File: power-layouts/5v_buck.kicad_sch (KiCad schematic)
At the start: 24 parts, among them U801 MIC28517T-E/PHA

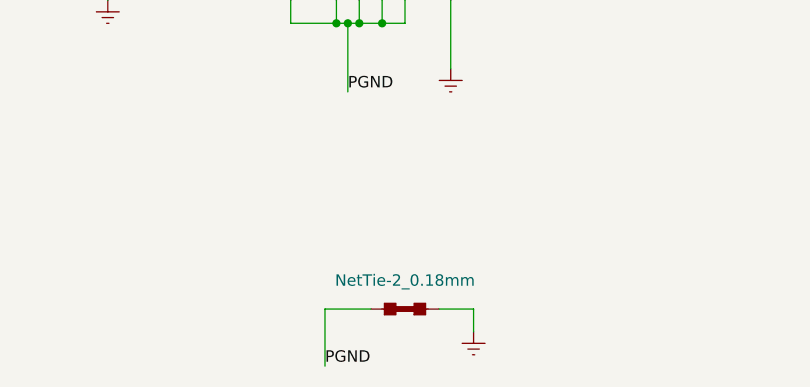
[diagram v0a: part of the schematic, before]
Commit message: Clean up silkscreen on power layouts
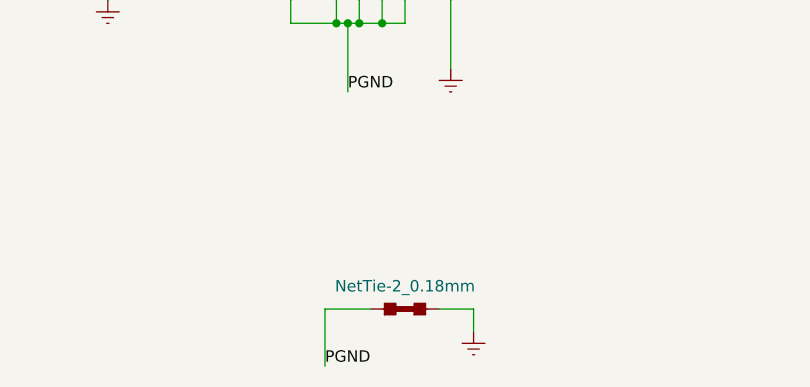
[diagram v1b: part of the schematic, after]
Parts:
- NT801: footprint BR_Virtual_Parts:NetTie-2_SMD_Pad_0.18mm_wide_long -> BR_Virtual_Parts:NetTie-2_SMD_Pad_3.88mm_wide; symbol BR_Virtual_Parts:NetTie-2_0.18mm_long -> BR_Virtual_Parts:NetTie-2_3.88mm
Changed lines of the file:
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@@
 	)
 	(symbol
-		(lib_id "BR_Virtual_Parts:NetTie-2_0.18mm_long")
+		(lib_id "BR_Virtual_Parts:NetTie-2_3.88mm")
 		(at 148.59 140.97 90)
 		(unit 1)
-		(exclude_from_sim no)
+		(exclude_from_sim yes)
 		(in_bom no)
 		(on_board yes)
@@
 		)
 		(property "Value" "NetTie-2_0.18mm"
-			(at 148.59 137.795 90)
+			(at 148.59 138.43 90)
 			(effects
 				(font
@@
 			)
 		)
-		(property "Footprint" "BR_Virtual_Parts:NetTie-2_SMD_Pad_0.18mm_wide_long"
-			(at 148.844 139.954 90)
+		(property "Footprint" "BR_Virtual_Parts:NetTie-2_SMD_Pad_3.88mm_wide"
+			(at 148.59 140.97 0)
 			(effects
 				(font
@@
 		)
 		(property "Datasheet" "~"
-			(at 143.51 132.08 0)
+			(at 148.59 140.97 0)
 			(effects
 				(font
@@
 		)
 		(property "Manufacturer" "~"
-			(at 129.54 138.43 0)
+			(at 148.59 140.97 0)
 			(effects
 				(font
 					(size 1.27 1.27)
 				)
-				(justify left)
 				(hide yes)
 			)
 		)
 		(property "Supplier 1" "~"
-			(at 127 138.43 0)
+			(at 148.59 140.97 0)
 			(effects
 				(font
 					(size 1.27 1.27)
 				)
-				(justify left)
 				(hide yes)
 			)
 		)
 		(property "Supplier Part Num 1" "~"
-			(at 124.46 138.43 0)
+			(at 148.59 140.97 0)
 			(effects
 				(font
 					(size 1.27 1.27)
 				)
-				(justify left)
 				(hide yes)
 			)
 		)
 		(property "Supplier 2" "~"
-			(at 121.92 138.43 0)
+			(at 148.59 140.97 0)
 			(effects
 				(font
 					(size 1.27 1.27)
 				)
-				(justify left)
 				(hide yes)
 			)
 		)
 		(property "Supplier Part Num 2" "~"
-			(at 119.38 138.43 0)
+			(at 148.59 140.97 0)
 			(effects
 				(font
 					(size 1.27 1.27)
 				)
-				(justify left)
 				(hide yes)
 			)
 		)
 		(property "Supplier 3" "~"
-			(at 116.84 138.43 0)
+			(at 148.59 140.97 0)
 			(effects
 				(font
 					(size 1.27 1.27)
 				)
-				(justify left)
 				(hide yes)
 			)
 		)
 		(property "Supplier Part Num 3" "~"
-			(at 114.3 138.43 0)
+			(at 148.59 140.97 0)
 			(effects
 				(font
 					(size 1.27 1.27)
 				)
-				(justify left)
 				(hide yes)
 			)
 		)
 		(property "Manufacturer Part Num" "~"
-			(at 111.76 138.43 0)
+			(at 148.59 140.97 0)
 			(effects
 				(font
 					(size 1.27 1.27)
 				)
-				(justify left)
 				(hide yes)
 			)
